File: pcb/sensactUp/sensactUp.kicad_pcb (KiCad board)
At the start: 2 copper layers, 71 x 71 mm, 93 parts, among them P1 CONN_01X06, P10 3V3, P11 CONN_02X05, P12 6/8, P13 5/L, P14 GND, P15 5V, P16 5V, P17 3V3, P18 24V_GND, P2 PWR, P3 CAN, P4 3V3, P5 ROT2EXT, P6 GND, P7 CONN_01X06, P8 24V_GND, P9 5V, Q1 Q_NMOS_GSD, Q2 Q_NMOS_GSD, Q3 Q_NMOS_GSD, Q4 Q_NMOS_GSD, SW1 ROTARY_ENCODER_SWITCH_CASE, SW2 RESET, U1 LMR14006, U2 LMR14006, U3 STM32F072C8Tx, U4 TLV70033DDC, U5 TJA1021T, U9 SN65HVD230, Y1 Crystal_GND24

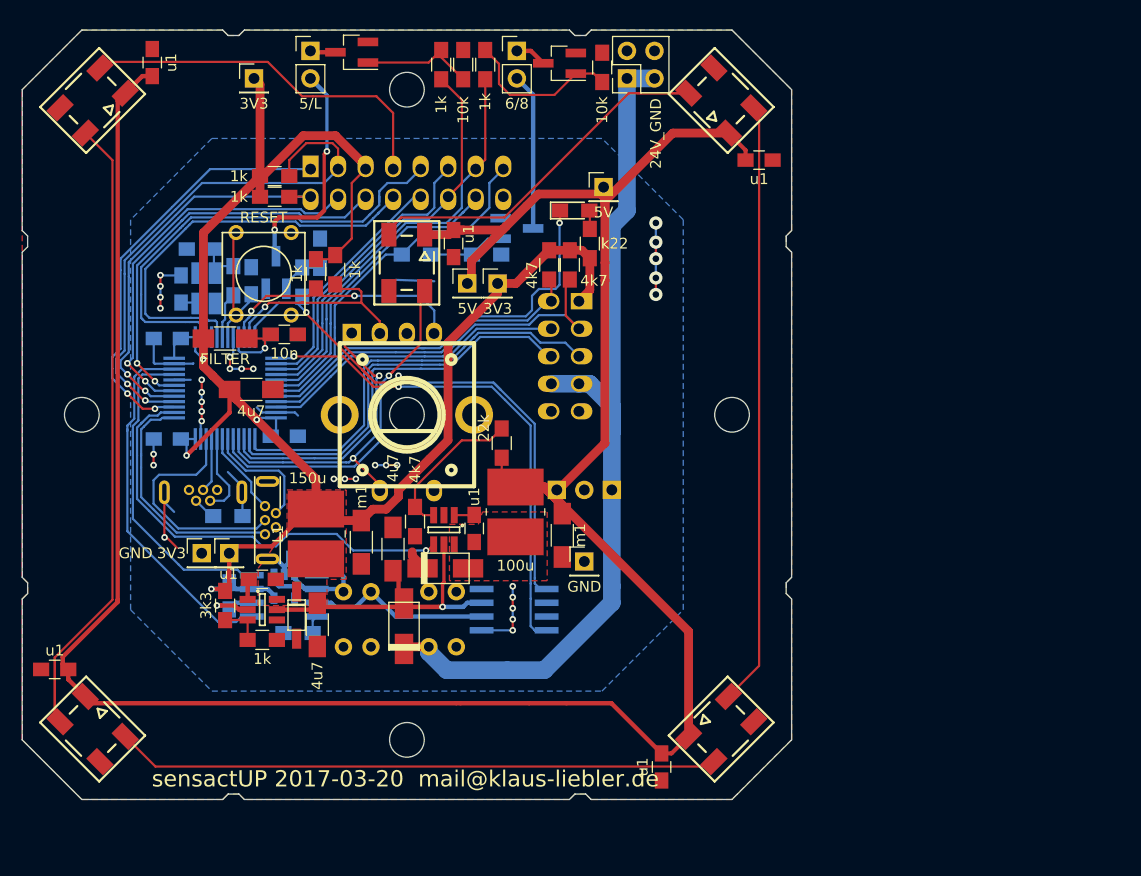
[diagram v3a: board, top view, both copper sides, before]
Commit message: sensactUP - going further
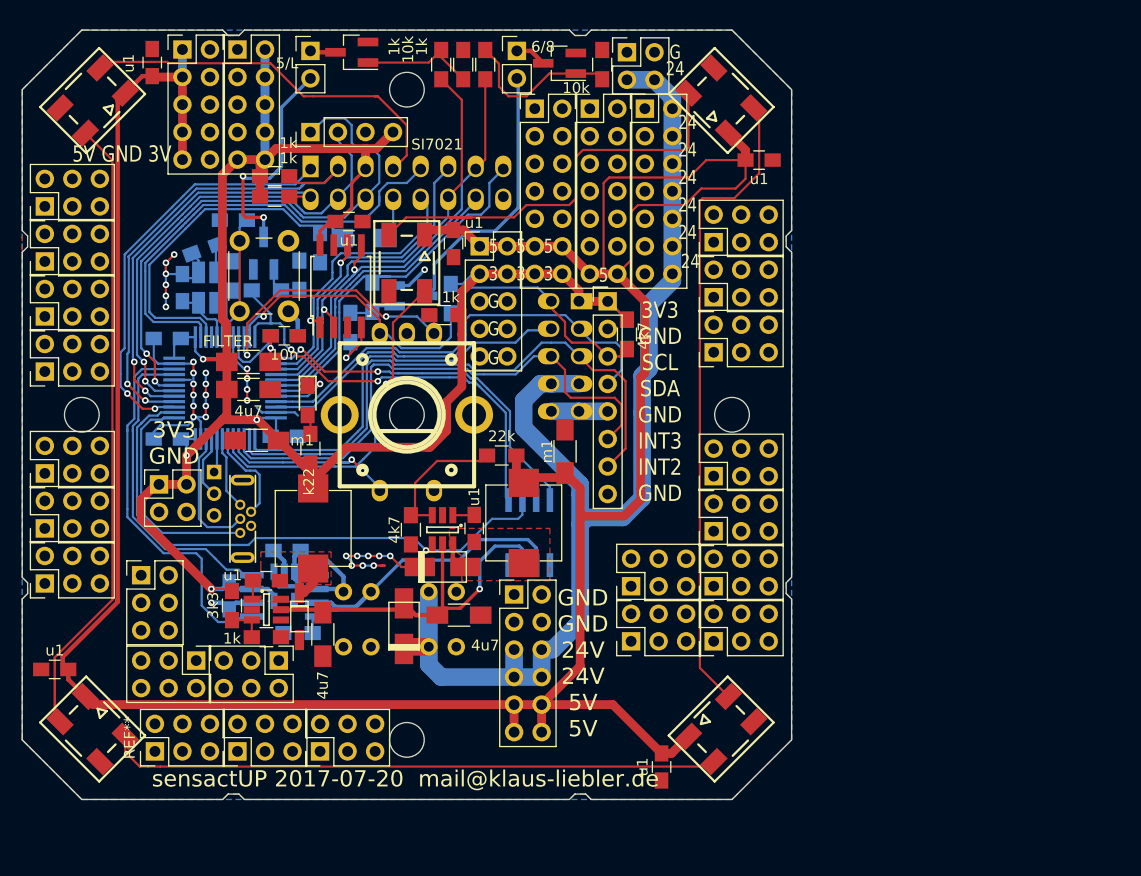
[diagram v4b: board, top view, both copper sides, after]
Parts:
- added C23: u1, Capacitors_SMD:C_0805_HandSoldering, F.Cu at (144.7, 82.2)
- added R23: 6k8, Resistors_SMD:R_1206_HandSoldering, B.Cu at (146.1, 83.7)
- added REF**: Pin_Header_Straight_2x03_Pitch2.54mm, Pin_Headers:Pin_Header_Straight_2x03_Pitch2.54mm, F.Cu at (116.6, 115.6)
- added REF**: Pin_Header_Straight_2x03_Pitch2.54mm, Pin_Headers:Pin_Header_Straight_2x03_Pitch2.54mm, F.Cu at (130.6, 122.7)
- added REF**: Pin_Header_Straight_2x03_Pitch2.54mm, Pin_Headers:Pin_Header_Straight_2x03_Pitch2.54mm, F.Cu at (138.2, 122.7)
- added REF**: Pin_Header_Straight_2x03_Pitch2.54mm, Pin_Headers:Pin_Header_Straight_2x03_Pitch2.54mm, F.Cu at (126.7, 131.1)
- added REF**: Pin_Header_Straight_2x03_Pitch2.54mm, Pin_Headers:Pin_Header_Straight_2x03_Pitch2.54mm, F.Cu at (134.4, 131.1)
- added REF**: Pin_Header_Straight_2x03_Pitch2.54mm, Pin_Headers:Pin_Header_Straight_2x03_Pitch2.54mm, F.Cu at (178.3, 120.9)
- added REF**: Pin_Header_Straight_2x03_Pitch2.54mm, Pin_Headers:Pin_Header_Straight_2x03_Pitch2.54mm, F.Cu at (142.0, 131.1)
- added REF**: Pin_Header_Straight_2x03_Pitch2.54mm, Pin_Headers:Pin_Header_Straight_2x03_Pitch2.54mm, F.Cu at (170.7, 115.8)
- added REF**: Pin_Header_Straight_2x03_Pitch2.54mm, Pin_Headers:Pin_Header_Straight_2x03_Pitch2.54mm, F.Cu at (178.3, 115.8)
- added REF**: Pin_Header_Straight_2x03_Pitch2.54mm, Pin_Headers:Pin_Header_Straight_2x03_Pitch2.54mm, F.Cu at (178.3, 110.7)
- added REF**: Pin_Header_Straight_2x03_Pitch2.54mm, Pin_Headers:Pin_Header_Straight_2x03_Pitch2.54mm, F.Cu at (178.3, 105.7)
- added REF**: Pin_Header_Straight_2x03_Pitch2.54mm, Pin_Headers:Pin_Header_Straight_2x03_Pitch2.54mm, F.Cu at (116.6, 110.5)
- added REF**: Pin_Header_Straight_2x03_Pitch2.54mm, Pin_Headers:Pin_Header_Straight_2x03_Pitch2.54mm, F.Cu at (178.3, 94.2)
- added REF**: Pin_Header_Straight_2x03_Pitch2.54mm, Pin_Headers:Pin_Header_Straight_2x03_Pitch2.54mm, F.Cu at (178.3, 89.2)
- added REF**: Pin_Header_Straight_2x03_Pitch2.54mm, Pin_Headers:Pin_Header_Straight_2x03_Pitch2.54mm, F.Cu at (178.3, 84.1)
- added REF**: Pin_Header_Straight_2x03_Pitch2.54mm, Pin_Headers:Pin_Header_Straight_2x03_Pitch2.54mm, F.Cu at (116.6, 105.4)
- added REF**: Pin_Header_Straight_2x03_Pitch2.54mm, Pin_Headers:Pin_Header_Straight_2x03_Pitch2.54mm, F.Cu at (116.6, 96.0)
- added REF**: Pin_Header_Straight_2x03_Pitch2.54mm, Pin_Headers:Pin_Header_Straight_2x03_Pitch2.54mm, F.Cu at (116.6, 90.9)
- added REF**: Pin_Header_Straight_2x03_Pitch2.54mm, Pin_Headers:Pin_Header_Straight_2x03_Pitch2.54mm, F.Cu at (116.6, 85.9)
- added REF**: Pin_Header_Straight_2x03_Pitch2.54mm, Pin_Headers:Pin_Header_Straight_2x03_Pitch2.54mm, F.Cu at (116.6, 80.8)
- added REF**: Pin_Header_Straight_2x03_Pitch2.54mm, Pin_Headers:Pin_Header_Straight_2x03_Pitch2.54mm, F.Cu at (170.7, 120.9)
- added REF**: Pin_Header_Straight_2x03_Pitch2.54mm, Pin_Headers:Pin_Header_Straight_2x03_Pitch2.54mm, F.Cu at (125.5, 114.8)
- added U6: M25PX32-VMW, sensact:SOIJ-8_5.3x5.3mm_Pitch1.27mm_handsolder, F.Cu at (143.9, 88.1)
- L1, L2: footprint sensact:SRR4028 -> sensact:PowerInductor_7mm
- P10, P4: value 3V3 -> CONN_02X05; footprint Pin_Headers:Pin_Header_Straight_1x01_Pitch2.54mm -> Pin_Headers:Pin_Header_Straight_2x05_Pitch2.54mm
- P14: value GND -> CONN_02X06; footprint Pin_Headers:Pin_Header_Straight_1x01_Pitch2.54mm -> Pin_Headers:Pin_Header_Straight_2x06_Pitch2.54mm
- P15: value 5V -> CONN_02X07; footprint Pin_Headers:Pin_Header_Straight_1x01_Pitch2.54mm -> Pin_Headers:Pin_Header_Straight_2x07_Pitch2.54mm
- P16: value 5V -> CONN_02X07; footprint Pin_Headers:Pin_Header_Straight_1x01_Pitch2.54mm -> Pin_Headers:Pin_Header_Straight_2x07_Pitch2.54mm; moved to F.Cu
- P17: value 3V3 -> CONN_02X07; footprint Pin_Headers:Pin_Header_Straight_1x01_Pitch2.54mm -> Pin_Headers:Pin_Header_Straight_2x07_Pitch2.54mm
- P18: value 24V_GND -> SI7021; footprint Pin_Headers:Pin_Header_Straight_1x02_Pitch2.54mm -> Pin_Headers:Pin_Header_Straight_1x04_Pitch2.54mm; moved to F.Cu
- P5: value ROT2EXT -> CONN_02X02; footprint Pin_Headers:Pin_Header_Straight_1x01_Pitch2.54mm -> Pin_Headers:Pin_Header_Straight_2x02_Pitch2.54mm; moved to F.Cu
- P6: value GND -> CONN_02X05; footprint Pin_Headers:Pin_Header_Straight_1x01_Pitch2.54mm -> Pin_Headers:Pin_Header_Straight_2x05_Pitch2.54mm
- P7: value CONN_01X06 -> USB; footprint sensact:MicroUsbVertical -> Pin_Headers:Pin_Header_Straight_1x03_Pitch2.00mm
- P8: value 24V_GND -> CONN_02X02
- P9: value 5V -> CCS811; footprint Pin_Headers:Pin_Header_Straight_1x01_Pitch2.54mm -> Pin_Headers:Pin_Header_Straight_1x08_Pitch2.54mm
- R10: value M1 -> 1k
- R13, R8: moved to B.Cu
- SW2: footprint Discret:SW_PUSH_SMALL -> Buttons_Switches_THT:SW_PUSH_6mm
- U4: footprint TO_SOT_Packages_SMD:SOT-23-5 -> sensact:SOT-23-5_handsolder
- moved P8 57.2 mm to (127.1, 106.4), turned to 0 degrees
- moved P6 46.5 mm to (129.3, 66.3)
- moved P10 46.5 mm to (134.4, 66.3)
- moved P18 43.2 mm to (141.1, 73.9)
- moved P5 36.3 mm to (170.3, 66.5), turned to 0 degrees
- moved P16 36.1 mm to (172.0, 71.8)
- moved R9 32.0 mm to (141.1, 103.1)
- moved D9 30.2 mm to (140.8, 98.7), turned to 270 degrees
- moved R10 26.2 mm to (142.0, 84.6), turned to 270 degrees
- moved P17 26.1 mm to (161.8, 71.8)
- moved R16 14.3 mm to (144.8, 91.9), turned to 270 degrees
- moved C1 13.5 mm to (136.1, 102.4), turned to 180 degrees
- moved P9 13.1 mm to (168.5, 89.5)
- moved R15 12.4 mm to (153.4, 90.8), turned to 180 degrees
- moved Q1 11.6 mm to (150.4, 89.0)
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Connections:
- O1 pad 8: IO1 -> /24Vin
- P10 pad 1: +3V3 -> GND
- P15 pad 1: +5V -> (no net)
- P16 pad 1: +5V -> (no net)
- P17 pad 1: +3V3 -> (no net)
- P18 pad 1: /24VX -> SDA1
- P18 pad 2: GND -> SCL1
- P2 pad 2: (no net) -> /24VX
- P4 pad 1: +3V3 -> +5V
- P5 pad 1: ROTD -> GND
- P6 pad 1: GND -> +5V
- P7 pad 1: (no net) -> /cpu/USBM
- P7 pad 2: /cpu/USBM -> /cpu/USBP
- P7 pad 3: /cpu/USBP -> GND
- P8 pad 1: /24VX -> +3V3
- P8 pad 2: GND -> +3V3
- P8 pad 3: /24VX -> GND
- P9 pad 1: +5V -> +3V3
- R10 pad 1: Net-(P7-Pad4) -> IO1
- U5 pad 2: (no net) -> SHDN
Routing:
- net +5V: track 239.5 -> 322.4 mm
- net /cpu/LED: track 38.3 -> 5.75 mm
- net /24VX: track 83.4 -> 108.4 mm
- net GND: track 63.2 -> 83.0 mm, vias 22 -> 32
- net LINRX: track 48.5 -> 34.0 mm
- net SDA1: track 37.5 -> 51.9 mm
- net (no net): track 14.2 -> 0.00 mm, vias 11 -> 0
- net +3V3: track 172.6 -> 186.8 mm
- net INT2: track 40.4 -> 54.4 mm
- net INT3: track 38.4 -> 51.2 mm
- net ROTD: track 30.7 -> 18.0 mm
- net SCL: track 31.7 -> 44.1 mm
- net SHDN: track 41.3 -> 53.3 mm
- net /O24_1: track 14.5 -> 25.1 mm
- net LINTX: track 51.2 -> 41.3 mm
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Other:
- board text added: "24"
- board text added: "3"
- board text added: "3V3 GND"
- board text added: "3V3 GND SCL SDA GND INT3 INT2 GND"
- board text added: "5"
- board text added: "5V GND 3V"
- board text added: "G"
- board text added: "GND GND 24V 24V 5V 5V"
- board text added: "sensactUP 2017-07-20 mail@klaus-liebler.de"
- board text added: "xRB xRD SC1 xRA SD1 3V3 IO1 WS1 IO3 IO2 IO5 IO4 IO7 IO6 GND IO8"
- board text removed: "sensactUP 2017-03-20 mail@klaus-liebler.de"
- board text removed: "xRD xRB xRA SC1 3V3 SD1 WS1 IO1 IO2 IO3 IO4 IO5 IO6 IO7 IO8 GND"

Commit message: PCB Order @ smart-prototyping 2017-07-26
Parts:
- added C24: 22p, Capacitors_SMD:C_0805_HandSoldering, B.Cu at (164.6, 113.5)
- added C25: u1, Capacitors_SMD:C_0805_HandSoldering, B.Cu at (161.3, 116.3)
- added P19: NWAKE, Wire_Pads:SolderWirePad_single_1mmDrill, F.Cu at (158.0, 103.1)
- added R24: 10k, Resistors_SMD:R_0805_HandSoldering, B.Cu at (158.9, 98.8)
- added REF**: Pin_Header_Straight_2x03_Pitch2.54mm, Pin_Headers:Pin_Header_Straight_2x03_Pitch2.54mm, F.Cu at (178.3, 92.5)
- added REF**: Pin_Header_Straight_2x03_Pitch2.54mm, Pin_Headers:Pin_Header_Straight_2x03_Pitch2.54mm, F.Cu at (178.3, 117.3)
- added REF**: Pin_Header_Straight_2x03_Pitch2.54mm, Pin_Headers:Pin_Header_Straight_2x03_Pitch2.54mm, F.Cu at (165.1, 129.3)
- P14: value CONN_02X06 -> CONN_02X05; footprint Pin_Headers:Pin_Header_Straight_2x06_Pitch2.54mm -> Pin_Headers:Pin_Header_Straight_2x05_Pitch2.54mm
- R7: value 220R -> k22
- moved REF** 13.0 mm to (178.3, 107.2)
- moved REF** 9.96 mm to (168.9, 119.1)
- moved REF** 9.96 mm to (168.9, 114.0)
- moved REF** 6.60 mm to (178.3, 112.3)
- moved REF** 6.49 mm to (165.1, 124.2)
- moved REF** 6.19 mm to (172.7, 121.7), turned to 0 degrees
- moved C4 4.06 mm to (152.1, 110.5)
- moved R3 4.06 mm to (146.3, 110.6)
- moved U1 3.83 mm to (149.5, 110.2)
- moved R2 3.81 mm to (158.8, 107.6)
- moved D1 3.81 mm to (149.5, 114.0)
- moved L2 3.45 mm to (158.0, 112.0), turned to 180 degrees
- moved REF** 2.29 mm to (178.3, 81.8)
- moved REF** 2.03 mm to (178.3, 87.1)
- moved P14 1.99 mm to (159.0, 118.4)
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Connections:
- P10 pad 5: GND -> (no net)
- P10 pad 7: GND -> (no net)
- P14 pad 3: GND -> /24VX
- P14 pad 4: GND -> /24VX
- P14 pad 7: /24VX -> +5V
- P14 pad 8: /24VX -> +5V
- P6 pad 10: GND -> (no net)
- P6 pad 5: +5V -> (no net)
- P6 pad 6: GND -> (no net)
- P6 pad 7: +5V -> (no net)
- P6 pad 8: GND -> (no net)
- P6 pad 9: +5V -> (no net)
- U5 pad 3: GND -> Net-(P19-Pad1)
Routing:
- net +5V: track 322.4 -> 241.6 mm
- net GND: track 83.0 -> 97.7 mm, vias 32 -> 34
- net Net-(P19-Pad1): track 0.00 -> 6.82 mm
- net /CANL_5V: track 14.8 -> 11.0 mm
- net /CANH_LIN: track 24.9 -> 28.1 mm
- net /SW5V: track 2.74 -> 0.00 mm
- net +24V: track 37.8 -> 35.2 mm
- net +3V3: track 186.8 -> 189.3 mm, vias 4 -> 5
- net LINTX: track 41.3 -> 39.4 mm
- net Net-(Q3-Pad1): track 10.8 -> 9.01 mm
- net SWDIO: track 12.1 -> 10.4 mm
- net IO8: track 35.3 -> 36.9 mm
- net Net-(D7-Pad2): track 60.3 -> 61.8 mm
- net SHDN: track 53.3 -> 51.9 mm
- net /O24_1: track 25.1 -> 26.6 mm
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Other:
- board text added: "2"
- board text added: "Für meine Familie, ich denke an Euch! Ich liebe Euch! Stefanie Klara "Würmchen""
- board text added: "sensactUP 2017-07-26 mail@klaus-liebler.de"
- board text removed: "GND GND 24V 24V 5V 5V"
- board text removed: "sensactUP 2017-07-20 mail@klaus-liebler.de"

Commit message: Fixed label on sensactUP04
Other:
- board text added: "xRD xRB xRA SC1 3V3 SD1 WS1 IO1 IO2 IO3 IO4 IO5 IO6 IO7 IO8 GND"
- board text removed: "xRB xRD SC1 xRA SD1 3V3 IO1 WS1 IO3 IO2 IO5 IO4 IO7 IO6 GND IO8"
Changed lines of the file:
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@@
     (34 B.Paste user)
     (35 F.Paste user)
-    (36 B.SilkS user hide)
+    (36 B.SilkS user)
     (37 F.SilkS user)
     (38 B.Mask user)
@@
     (tags "resistor 0805")
     (attr smd)
-    (fp_text reference R24 (at 0 1.7 270) (layer B.SilkS)
+    (fp_text reference R24 (at 0 1.7 270) (layer B.SilkS) hide
       (effects (font (size 1 1) (thickness 0.15)) (justify mirror))
     )
@@
   (gr_arc (start 167.5 117.5) (end 175.5 117.5) (angle 90) (layer Dwgs.User) (width 0.2))
   (gr_arc (start 167.5 82.5) (end 167.5 74.5) (angle 90) (layer Dwgs.User) (width 0.2))
-  (gr_text "xRB xRD\nSC1 xRA \nSD1 3V3\nIO1 WS1\n\nIO3 IO2\nIO5 IO4\nIO7 IO6\nGND IO8\n\n" (at 151.13 67.564 90) (layer B.SilkS)
+  (gr_text "xRD xRB\nxRA SC1 \n3V3 SD1\nWS1 IO1\n\nIO2 IO3\nIO4 IO5\nIO6 IO7\nIO8 GND\n\n" (at 151.13 67.564 90) (layer B.SilkS)
     (effects (font (size 1.2 0.8) (thickness 0.2)) (justify left mirror))
   )

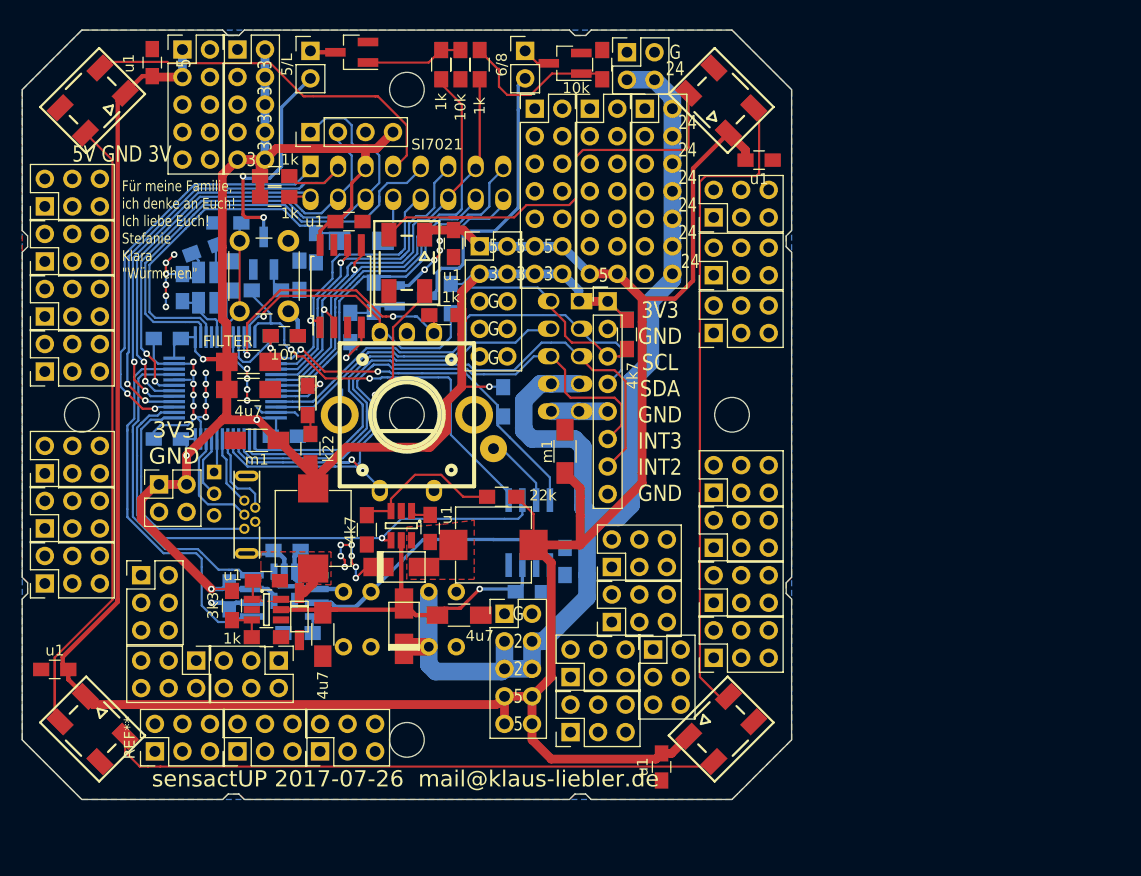
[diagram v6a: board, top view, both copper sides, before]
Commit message: Various changes as flashed to NODE_SNSCT_L0_TECH_HS_1
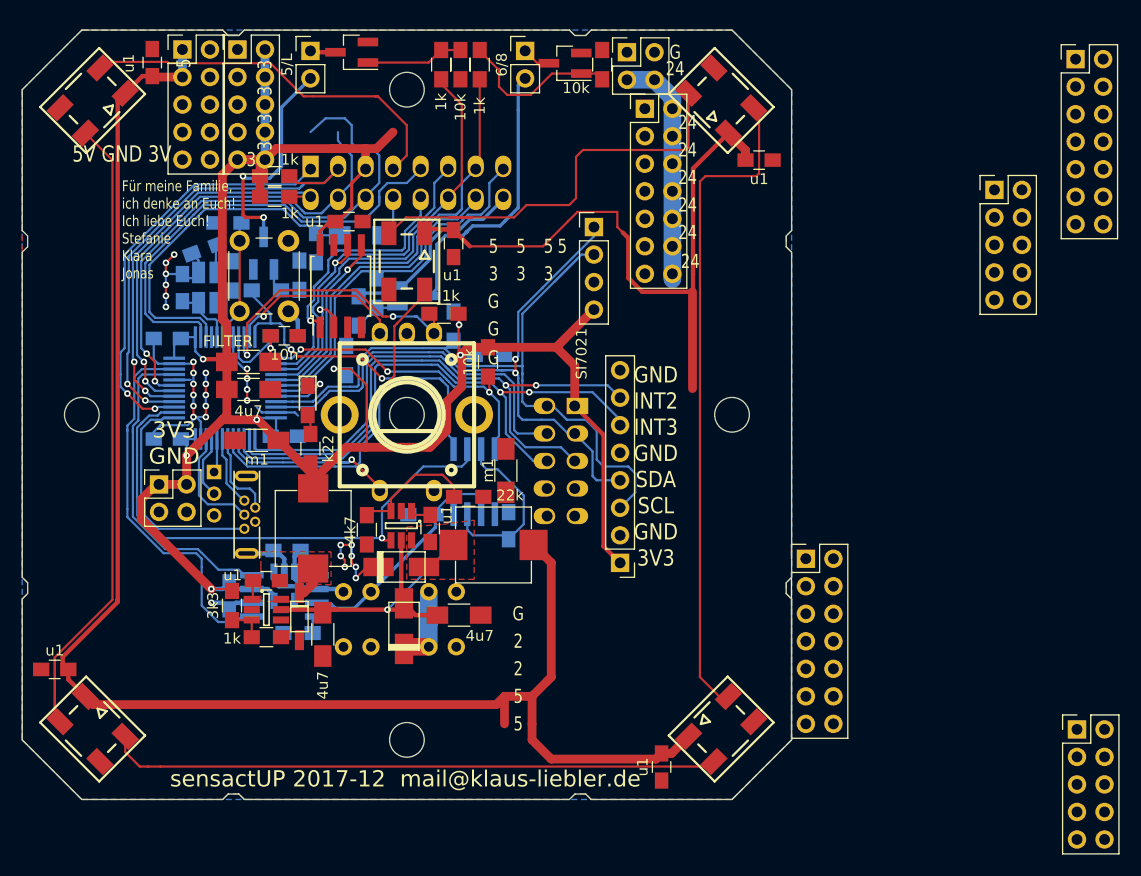
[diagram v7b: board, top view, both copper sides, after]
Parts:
- removed P19: NWAKE, Wire_Pads:SolderWirePad_single_1mmDrill
- removed REF** (x25): Pin_Header_Straight_2x03_Pitch2.54mm, Pin_Headers:Pin_Header_Straight_2x03_Pitch2.54mm
- R14: moved to B.Cu
- R24: moved to F.Cu
- R7: value k22 -> 220R
- moved P14 53.9 mm to (211.8, 129.0)
- moved P17 50.1 mm to (211.7, 67.2)
- moved P4 47.8 mm to (204.2, 79.2)
- moved P15 46.1 mm to (186.8, 113.3)
- moved P18 27.6 mm to (167.3, 82.7), turned to 0 degrees
- moved P9 24.2 mm to (169.7, 113.7), turned to 180 degrees
- moved R14 16.0 mm to (154.3, 91.8)
- moved C24 13.9 mm to (151.4, 109.2), turned to 180 degrees
- moved R8 12.8 mm to (157.6, 94.5), turned to 0 degrees
- moved R13 11.2 mm to (144.4, 95.0), turned to 90 degrees
- moved P11 9.67 mm to (164.2, 104.3)
- moved U5 6.92 mm to (156.2, 106.2)
- moved C25 6.39 mm to (159.4, 110.2), turned to 90 degrees
- moved C6 5.74 mm to (159.1, 105.2)
- moved R24 3.94 mm to (157.5, 95.1)
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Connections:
- P18 pad 1: SDA1 -> SDA
- P18 pad 2: SCL1 -> SCL
- U5 pad 3: Net-(P19-Pad1) -> +24V
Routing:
- net /24VX: track 108.4 -> 29.5 mm
- net +5V: track 241.6 -> 214.2 mm
- net SCL: track 44.1 -> 67.3 mm
- net SDA: track 42.2 -> 62.9 mm, vias 0 -> 2
- net +3V3: track 189.3 -> 207.2 mm, vias 5 -> 7
- net +24V: track 35.2 -> 52.2 mm
- net GND: track 97.7 -> 87.6 mm, vias 34 -> 29
- net LINTX: track 39.4 -> 32.3 mm
- net Net-(P19-Pad1): track 6.82 -> 0.00 mm
- net ROTB: track 26.4 -> 20.2 mm
- net LINRX: track 34.9 -> 28.9 mm, vias 2 -> 3
- net /CANH_LIN: track 28.1 -> 22.2 mm
- net WS2812: track 35.1 -> 32.0 mm
- net IO8: track 36.9 -> 39.7 mm
- net Net-(R2-Pad2): track 14.1 -> 11.7 mm
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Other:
- board text added: "Für meine Familie, ich denke an Euch! Ich liebe Euch! Stefanie Klara Jonas"
- board text added: "GND INT2 INT3 GND SDA SCL GND 3V3"
- board text added: "sensactUP 2017-12 mail@klaus-liebler.de"
- board text removed: "3V3 GND SCL SDA GND INT3 INT2 GND"
- board text removed: "Für meine Familie, ich denke an Euch! Ich liebe Euch! Stefanie Klara "Würmchen""
- board text removed: "sensactUP 2017-07-26 mail@klaus-liebler.de"

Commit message: FirmwareUpdate auf CubeMX 24
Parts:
- removed P8: CONN_02X02, Pin_Headers:Pin_Header_Straight_2x02_Pitch2.54mm
- removed U3: STM32F072C8Tx, sensact:LQFP-48_7x7mm_Pitch0.5mm_handsolder
- added REF**: WAGO 250-208, WestfaelischeHochschule:WAGO 250-208, F.Cu at (195.0, 71.0)
- added REF**: ESP32-WROOM, ESP32:ESP32-WROOM, F.Cu at (159.0, 86.0)
- moved SW1 17.0 mm to (162.0, 112.0)
- moved P11 11.7 mm to (161.0, 93.0)
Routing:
- net (no net): track 0.00 -> 41.5 mm, vias 0 -> 3
- net ROTA: track 26.8 -> 2.00 mm, vias 2 -> 0
- net ROTB: track 20.2 -> 3.58 mm, vias 1 -> 0
